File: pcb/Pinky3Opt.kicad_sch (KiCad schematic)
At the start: 17 parts, among them J1 USB_C_Receptacle_USB2.0, SW1 SW_Push, U1 ATmega32U4-A, Y1 16MHz

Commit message: left hand schematic
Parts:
- added C8: 10uF, symbol Device:C_Small
- added D1, D10, D11, D12, D13, D14, D15, D16, D17, D18, D19, D2, D20, D21, D22, D23, D24, D25, D3, D4, D5, D6, D7, D8, D9: D, symbol Device:D
- added D26: D_Schottky, symbol Device:D_Schottky
- added F1: 500mA, symbol Device:Polyfuse
- added J2: Conn_01x04, symbol Connector_Generic:Conn_01x04
- added MX1, MX10, MX11, MX12, MX13, MX14, MX15, MX16, MX17, MX18, MX19, MX2, MX20, MX21, MX22, MX23, MX24, MX25, MX3, MX4, MX5, MX6, MX7, MX8, MX9: MX-NoLED, symbol MX_Alps_Hybrid:MX-NoLED
- added R7, R8: 4.7k, symbol Device:R_Small
- added R9: 10k, symbol Device:R_Small
- added U2: PRTR5V0U2X, symbol random-keyboard-parts:PRTR5V0U2X
- C5: value 10uF -> 0.1uF
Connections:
- net +5V: now also D26.1 (K), J2.4 (Pin_4), R7.1, R8.1, R9.2; no longer J1.A4 (VBUS), J1.A9 (VBUS), J1.B4 (VBUS), J1.B9 (VBUS), U1.2 (UVCC)
- net D+: now also R2.2, U1.4 (D+); no longer J1.A6 (D+), J1.B6 (D+), R2.1
- net D-: now also R3.2, U1.3 (D-); no longer J1.A7 (D-), J1.B7 (D-), R3.1
- net GND: now also C8.2, J2.1 (Pin_1), U2.1 (GND)
- net SCL: now reaches U1.18 (PD0)
- net SCL: now also J2.2 (Pin_2), R7.2
- net SDA: now reaches U1.19 (PD1)
- net SDA: now also J2.3 (Pin_3), R8.2
- net HDETECT: now reaches U1.22 (PD5)
- net HDETECT: now also R9.1
- new net: D1.2 (A), MX1.2 (ROW)
- new net: D11.2 (A), MX11.2 (ROW)
- new net: D8.2 (A), MX8.2 (ROW)
- new net: D22.2 (A), MX22.2 (ROW)
- new net: J1.A6 (D+), J1.B6 (D+), R2.1, U2.2 (IO1)
- new net: J1.A7 (D-), J1.B7 (D-), R3.1, U2.3 (IO2)
- new net: D25.2 (A), MX25.2 (ROW)
- new net: D16.2 (A), MX16.2 (ROW)
- new net: D13.2 (A), MX13.2 (ROW)
- new net: D5.2 (A), MX5.2 (ROW)
- new net: D9.2 (A), MX9.2 (ROW)
- new net: D18.2 (A), MX18.2 (ROW)
- new net: D4.2 (A), MX4.2 (ROW)
- new net: D3.2 (A), MX3.2 (ROW)
- new net: D12.2 (A), MX12.2 (ROW)
- new net: D7.2 (A), MX7.2 (ROW)
- new net: D10.2 (A), MX10.2 (ROW)
- new net: D23.2 (A), MX23.2 (ROW)
- new net: D21.2 (A), MX21.2 (ROW)
- new net: D17.2 (A), MX17.2 (ROW)
- new net: D14.2 (A), MX14.2 (ROW)
- new net: D6.2 (A), MX6.2 (ROW)
- new net: D15.2 (A), MX15.2 (ROW)
- new net: D20.2 (A), MX20.2 (ROW)
- new net: D19.2 (A), MX19.2 (ROW)
- new net: D2.2 (A), MX2.2 (ROW)
- new net: D24.2 (A), MX24.2 (ROW)
- new net L_COL0: MX1.1 (COL), MX15.1 (COL), MX8.1 (COL)
- new net L_COL1: MX16.1 (COL), MX2.1 (COL), MX9.1 (COL)
- new net L_COL2: MX10.1 (COL), MX17.1 (COL), MX3.1 (COL)
- new net L_COL3: MX11.1 (COL), MX18.1 (COL), MX22.1 (COL), MX4.1 (COL)
- new net L_COL4: MX12.1 (COL), MX19.1 (COL), MX23.1 (COL), MX5.1 (COL)
- new net L_COL5: MX13.1 (COL), MX20.1 (COL), MX24.1 (COL), MX6.1 (COL)
- new net L_COL6: MX14.1 (COL), MX21.1 (COL), MX25.1 (COL), MX7.1 (COL)
- new net L_ROW0: D1.1 (K), D2.1 (K), D3.1 (K), D4.1 (K), D5.1 (K), D6.1 (K), D7.1 (K)
- new net L_ROW1: D10.1 (K), D11.1 (K), D12.1 (K), D13.1 (K), D14.1 (K), D8.1 (K), D9.1 (K)
- new net L_ROW2: D15.1 (K), D16.1 (K), D17.1 (K), D18.1 (K), D19.1 (K), D20.1 (K), D21.1 (K)
- new net L_ROW3: D22.1 (K), D23.1 (K), D24.1 (K), D25.1 (K)
- new net VBUS: C8.1, D26.2 (A), F1.2, U1.2 (UVCC)
- new net VCC: F1.1, J1.A4 (VBUS), J1.A9 (VBUS), J1.B4 (VBUS), J1.B9 (VBUS), U2.4 (VCC)
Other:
- moved on the sheet: C2, C3, C4, C5, J1, R5, R6

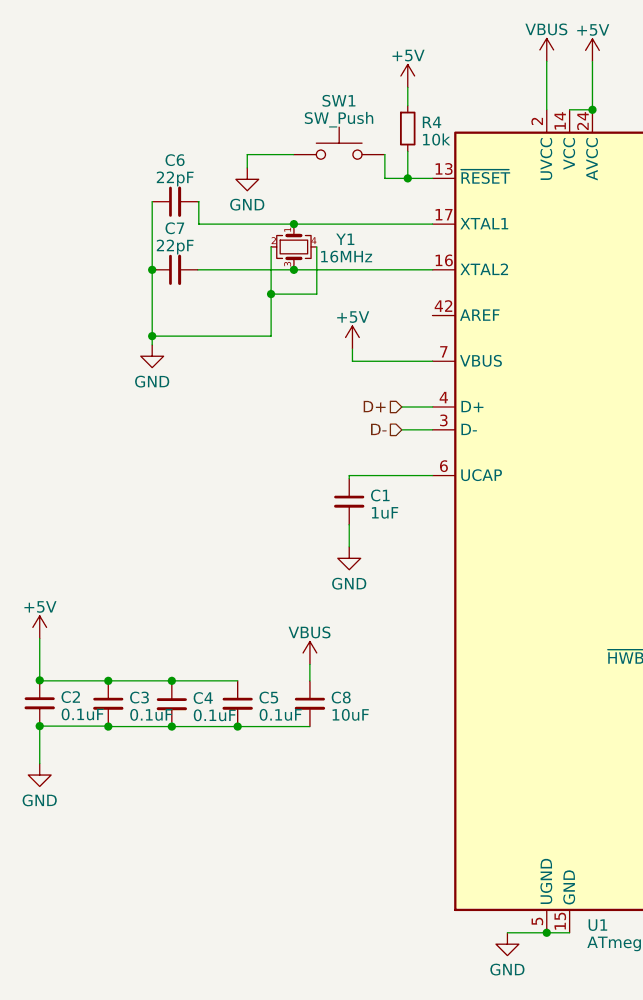
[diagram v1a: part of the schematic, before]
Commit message: fix erc error
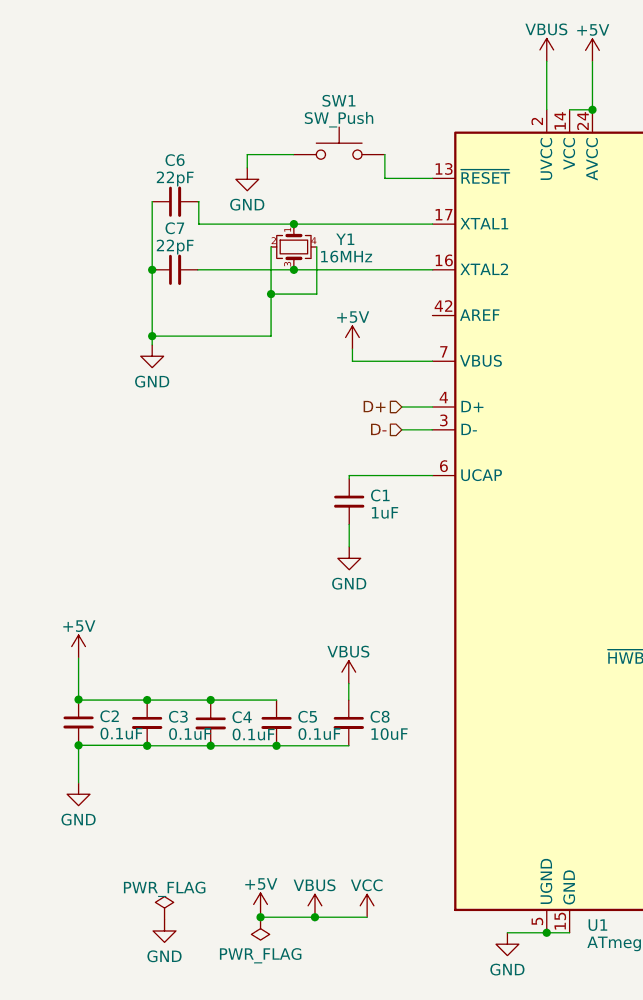
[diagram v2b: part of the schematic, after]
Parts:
- removed R4: 10k, symbol Device:R_Small
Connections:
- net VBUS is gone; now on net +5V: C8.1, D26.2 (A), F1.2, U1.2 (UVCC)
- net VCC is gone; now on net +5V: F1.1, J1.A4 (VBUS), J1.A9 (VBUS), J1.B4 (VBUS), J1.B9 (VBUS), U2.4 (VCC)
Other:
- moved on the sheet: C2, C3, C4, C5, C8

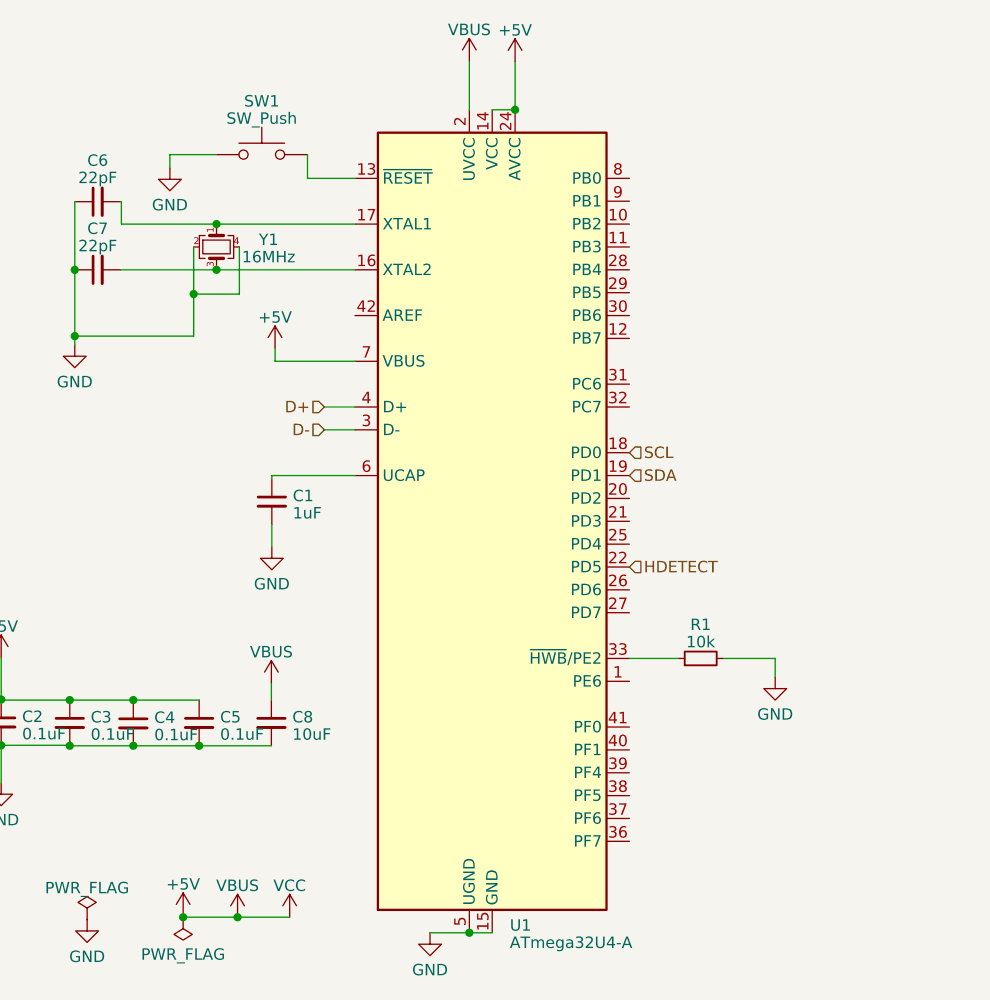
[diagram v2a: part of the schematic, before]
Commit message: rows and cols to mcu
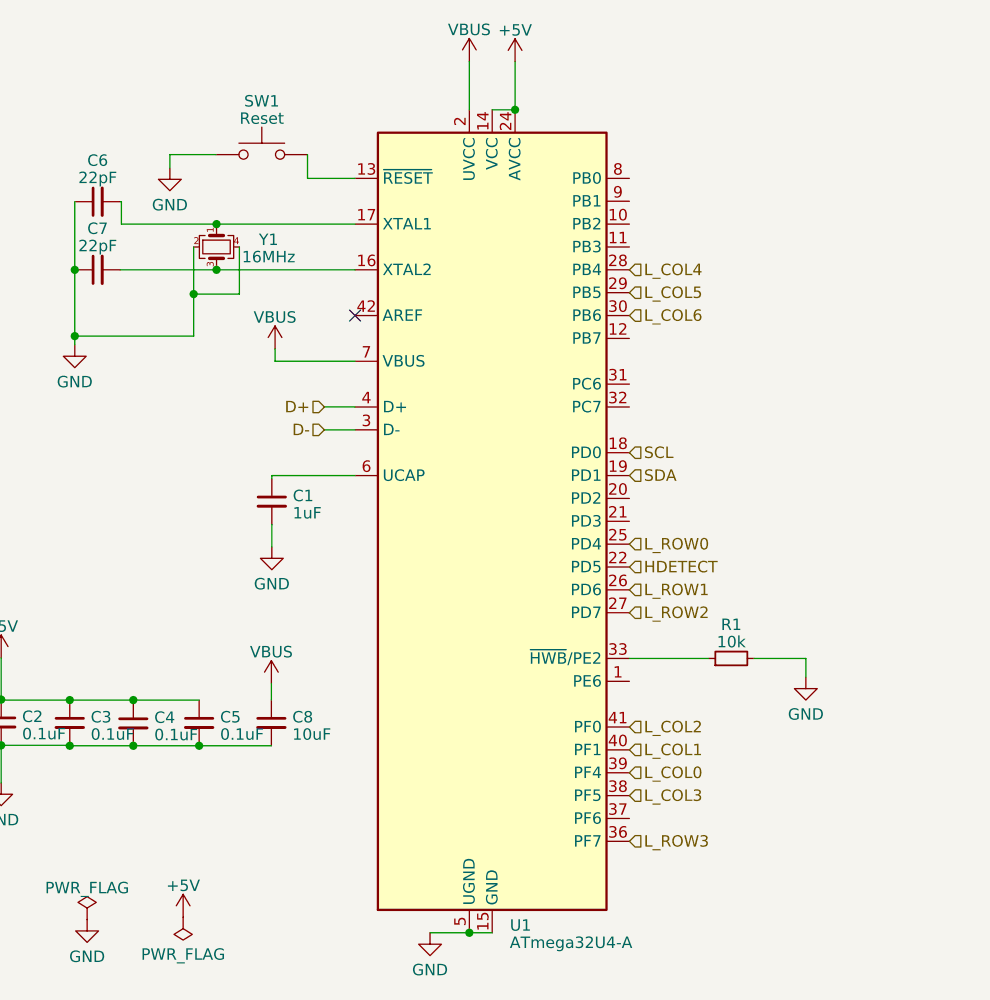
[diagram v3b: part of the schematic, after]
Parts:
- C1, C2, C3, C4, C5, C6, C7, C8: footprint (none) -> Capacitor_SMD:C_0805_2012Metric
- D1, D10, D11, D12, D13, D14, D15, D16, D17, D18, D19, D2, D20, D21, D22, D23, D24, D25, D26, D3, D4, D5, D6, D7, D8, D9: footprint (none) -> Diode_SMD:D_SOD-123
- F1: footprint (none) -> Fuse:Fuse_1206_3216Metric
- J1: footprint (none) -> Connector_USB:USB_C_Receptacle_HRO_TYPE-C-31-M-12
- J2: footprint (none) -> random-keyboard-parts:PJ-3200B-4A-Assembly
- MX1, MX10, MX11, MX12, MX13, MX14, MX15, MX16, MX17, MX18, MX19, MX2, MX20, MX21, MX3, MX4, MX5, MX6, MX7, MX8, MX9: footprint (none) -> kbd:CherryMX_Hotswap
- MX22, MX23, MX24, MX25: footprint (none) -> kbd:ChocV1_V2_Hotswap
- R1, R2, R3, R5, R6, R7, R8, R9: footprint (none) -> Resistor_SMD:R_0805_2012Metric
- SW1: value SW_Push -> Reset; footprint (none) -> random-keyboard-parts:SKQGADE010
- U2: footprint (none) -> random-keyboard-parts:SOT143B
- Y1: footprint (none) -> Crystal:Crystal_SMD_3225-4Pin_3.2x2.5mm
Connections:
- net +5V: no longer C8.1, D26.2 (A), F1.1, F1.2, J1.A4 (VBUS), J1.A9 (VBUS), J1.B4 (VBUS), J1.B9 (VBUS), U1.2 (UVCC), U1.7 (VBUS), U2.4 (VCC)
- net L_COL0: now also U1.39 (PF4)
- net L_COL1: now also U1.40 (PF1)
- net L_COL2: now also U1.41 (PF0)
- net L_COL3: now also U1.38 (PF5)
- net L_COL4: now also U1.28 (PB4)
- net L_COL5: now also U1.29 (PB5)
- net L_COL6: now also U1.30 (PB6)
- net L_ROW0: now also U1.25 (PD4)
- net L_ROW1: now also U1.26 (PD6)
- net L_ROW2: now also U1.27 (PD7)
- net L_ROW3: now also U1.36 (PF7)
- new net VBUS: C8.1, D26.2 (A), F1.2, U1.2 (UVCC), U1.7 (VBUS)
- new net VCC: F1.1, J1.A4 (VBUS), J1.A9 (VBUS), J1.B4 (VBUS), J1.B9 (VBUS), U2.4 (VCC)
- no-connect marks 2 -> 3
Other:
- moved on the sheet: R1

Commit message: maybe done left hand
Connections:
- net HDETECT renamed HDETECT_L
- net L_COL0 renamed COL0_L
- net L_COL1 renamed COL1_L
- net L_COL2 renamed COL2_L
- net L_COL3 renamed COL3_L
- net L_COL4 renamed COL4_L
- net L_COL5 renamed COL5_L
- net L_COL6 renamed COL6_L
- net L_ROW0 renamed ROW0_L
- net L_ROW1 renamed ROW1_L
- net L_ROW2 renamed ROW2_L
- net L_ROW3 renamed ROW3_L
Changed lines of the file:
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@@
     (effects (font (size 1.27 1.27)) (justify right))
   )
-  (hierarchical_label "L_ROW1" (shape input) (at 259.2832 72.3392 180) (fields_autoplaced)
+  (hierarchical_label "ROW1_L" (shape input) (at 259.2832 72.3392 180) (fields_autoplaced)
     (effects (font (size 1.27 1.27)) (justify right))
   )
-  (hierarchical_label "L_COL5" (shape input) (at 351.8408 33.2232 90) (fields_autoplaced)
+  (hierarchical_label "COL5_L" (shape input) (at 351.8408 33.2232 90) (fields_autoplaced)
     (effects (font (size 1.27 1.27)) (justify left))
   )
-  (hierarchical_label "L_COL6" (shape input) (at 366.8268 33.274 90) (fields_autoplaced)
+  (hierarchical_label "COL6_L" (shape input) (at 366.8268 33.274 90) (fields_autoplaced)
     (effects (font (size 1.27 1.27)) (justify left))
   )
-  (hierarchical_label "L_COL0" (shape input) (at 96.7232 102.5144 0) (fields_autoplaced)
+  (hierarchical_label "COL0_L" (shape input) (at 96.7232 102.5144 0) (fields_autoplaced)
     (effects (font (size 1.27 1.27)) (justify left))
   )
-  (hierarchical_label "L_ROW3" (shape input) (at 96.7232 110.1344 0) (fields_autoplaced)
+  (hierarchical_label "ROW3_L" (shape input) (at 96.7232 110.1344 0) (fields_autoplaced)
     (effects (font (size 1.27 1.27)) (justify left))
   )
-  (hierarchical_label "L_ROW2" (shape input) (at 96.7232 84.7344 0) (fields_autoplaced)
+  (hierarchical_label "ROW2_L" (shape input) (at 96.7232 84.7344 0) (fields_autoplaced)
     (effects (font (size 1.27 1.27)) (justify left))
   )
@@
     (effects (font (size 1.27 1.27)) (justify left))
   )
-  (hierarchical_label "L_ROW3" (shape input) (at 307.4924 118.1608 180) (fields_autoplaced)
+  (hierarchical_label "ROW3_L" (shape input) (at 307.4924 118.1608 180) (fields_autoplaced)
     (effects (font (size 1.27 1.27)) (justify right))
   )
-  (hierarchical_label "L_COL1" (shape input) (at 288.9504 32.9184 90) (fields_autoplaced)
+  (hierarchical_label "COL1_L" (shape input) (at 288.9504 32.9184 90) (fields_autoplaced)
     (effects (font (size 1.27 1.27)) (justify left))
   )
-  (hierarchical_label "HDETECT" (shape input) (at 195.7832 96.1644 180) (fields_autoplaced)
+  (hierarchical_label "HDETECT_L" (shape input) (at 195.7832 96.1644 180) (fields_autoplaced)
     (effects (font (size 1.27 1.27)) (justify right))
   )
@@
     (effects (font (size 1.27 1.27)) (justify right))
   )
-  (hierarchical_label "L_COL0" (shape input) (at 273.4056 33.1216 90) (fields_autoplaced)
+  (hierarchical_label "COL0_L" (shape input) (at 273.4056 33.1216 90) (fields_autoplaced)
     (effects (font (size 1.27 1.27)) (justify left))
   )
-  (hierarchical_label "L_COL4" (shape input) (at 96.7232 46.6344 0) (fields_autoplaced)
+  (hierarchical_label "COL4_L" (shape input) (at 96.7232 46.6344 0) (fields_autoplaced)
     (effects (font (size 1.27 1.27)) (justify left))
   )
-  (hierarchical_label "L_COL1" (shape input) (at 96.7232 99.9744 0) (fields_autoplaced)
+  (hierarchical_label "COL1_L" (shape input) (at 96.7232 99.9744 0) (fields_autoplaced)
     (effects (font (size 1.27 1.27)) (justify left))
   )
@@
     (effects (font (size 1.27 1.27)) (justify right))
   )
-  (hierarchical_label "L_COL2" (shape input) (at 96.7232 97.4344 0) (fields_autoplaced)
+  (hierarchical_label "COL2_L" (shape input) (at 96.7232 97.4344 0) (fields_autoplaced)
     (effects (font (size 1.27 1.27)) (justify left))
   )
-  (hierarchical_label "L_COL6" (shape input) (at 96.7232 51.7144 0) (fields_autoplaced)
+  (hierarchical_label "COL6_L" (shape input) (at 96.7232 51.7144 0) (fields_autoplaced)
     (effects (font (size 1.27 1.27)) (justify left))
   )
@@
     (effects (font (size 1.27 1.27)) (justify right))
   )
-  (hierarchical_label "L_COL3" (shape input) (at 319.8368 32.9184 90) (fields_autoplaced)
+  (hierarchical_label "COL3_L" (shape input) (at 319.8368 32.9184 90) (fields_autoplaced)
     (effects (font (size 1.27 1.27)) (justify left))
   )
-  (hierarchical_label "L_COL3" (shape input) (at 96.7232 105.0544 0) (fields_autoplaced)
+  (hierarchical_label "COL3_L" (shape input) (at 96.7232 105.0544 0) (fields_autoplaced)
     (effects (font (size 1.27 1.27)) (justify left))
   )
-  (hierarchical_label "L_ROW1" (shape input) (at 96.7232 82.1944 0) (fields_autoplaced)
+  (hierarchical_label "ROW1_L" (shape input) (at 96.7232 82.1944 0) (fields_autoplaced)
     (effects (font (size 1.27 1.27)) (justify left))
   )
@@
     (effects (font (size 1.27 1.27)) (justify left))
   )
-  (hierarchical_label "HDETECT" (shape input) (at 96.7232 79.6544 0) (fields_autoplaced)
+  (hierarchical_label "HDETECT_L" (shape input) (at 96.7232 79.6544 0) (fields_autoplaced)
     (effects (font (size 1.27 1.27)) (justify left))
   )
@@
     (effects (font (size 1.27 1.27)) (justify left))
   )
-  (hierarchical_label "L_COL2" (shape input) (at 304.1904 32.9184 90) (fields_autoplaced)
+  (hierarchical_label "COL2_L" (shape input) (at 304.1904 32.9184 90) (fields_autoplaced)
     (effects (font (size 1.27 1.27)) (justify left))
   )
-  (hierarchical_label "L_ROW0" (shape input) (at 96.7232 77.1144 0) (fields_autoplaced)
+  (hierarchical_label "ROW0_L" (shape input) (at 96.7232 77.1144 0) (fields_autoplaced)
     (effects (font (size 1.27 1.27)) (justify left))
   )
-  (hierarchical_label "L_ROW2" (shape input) (at 258.9784 93.98 180) (fields_autoplaced)
+  (hierarchical_label "ROW2_L" (shape input) (at 258.9784 93.98 180) (fields_autoplaced)
     (effects (font (size 1.27 1.27)) (justify right))
   )
-  (hierarchical_label "L_ROW0" (shape input) (at 259.2832 52.2732 180) (fields_autoplaced)
+  (hierarchical_label "ROW0_L" (shape input) (at 259.2832 52.2732 180) (fields_autoplaced)
     (effects (font (size 1.27 1.27)) (justify right))
   )
-  (hierarchical_label "L_COL5" (shape input) (at 96.7232 49.1744 0) (fields_autoplaced)
+  (hierarchical_label "COL5_L" (shape input) (at 96.7232 49.1744 0) (fields_autoplaced)
     (effects (font (size 1.27 1.27)) (justify left))
   )
-  (hierarchical_label "L_COL4" (shape input) (at 336.6008 33.1724 90) (fields_autoplaced)
+  (hierarchical_label "COL4_L" (shape input) (at 336.6008 33.1724 90) (fields_autoplaced)
     (effects (font (size 1.27 1.27)) (justify left))
   )
